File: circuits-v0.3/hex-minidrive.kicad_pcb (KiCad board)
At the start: 4 copper layers, 18 x 48 mm, 81 parts, among them X1 16MHz

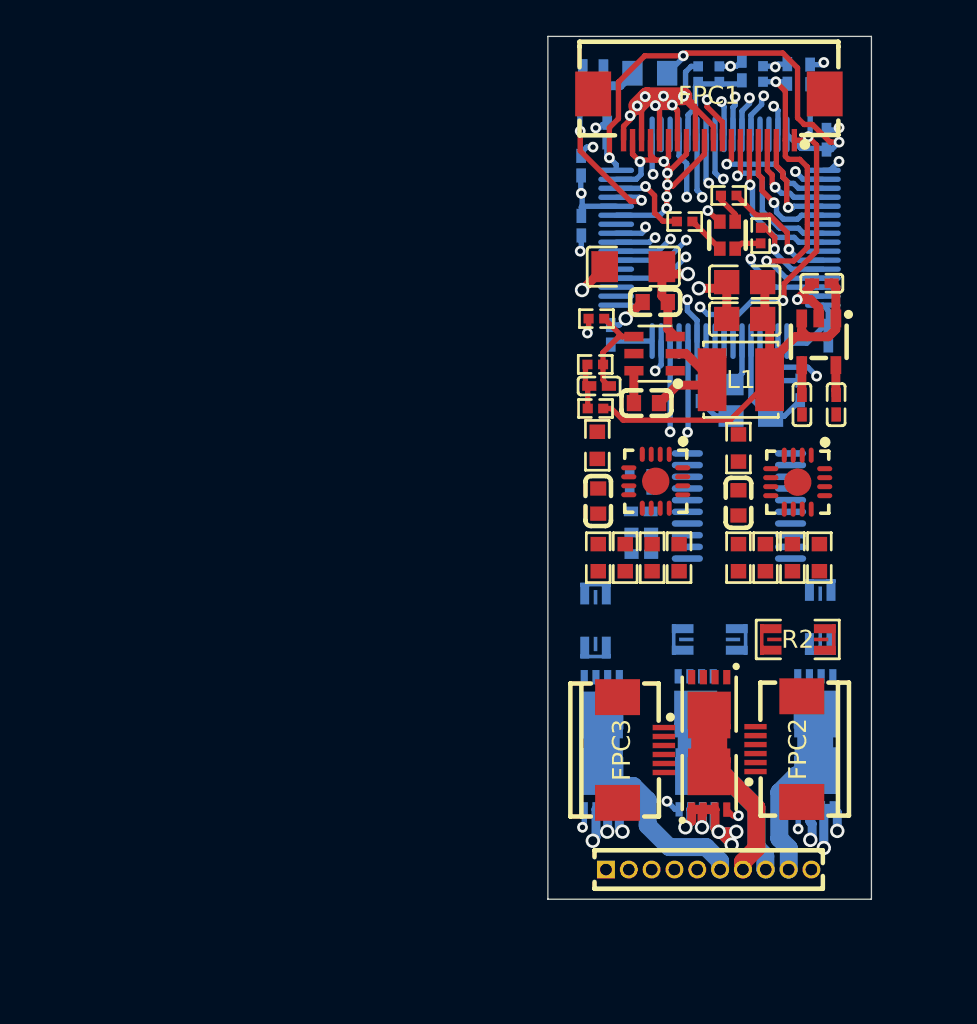
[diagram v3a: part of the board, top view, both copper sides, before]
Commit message: Sketch out route for all crossing wires.
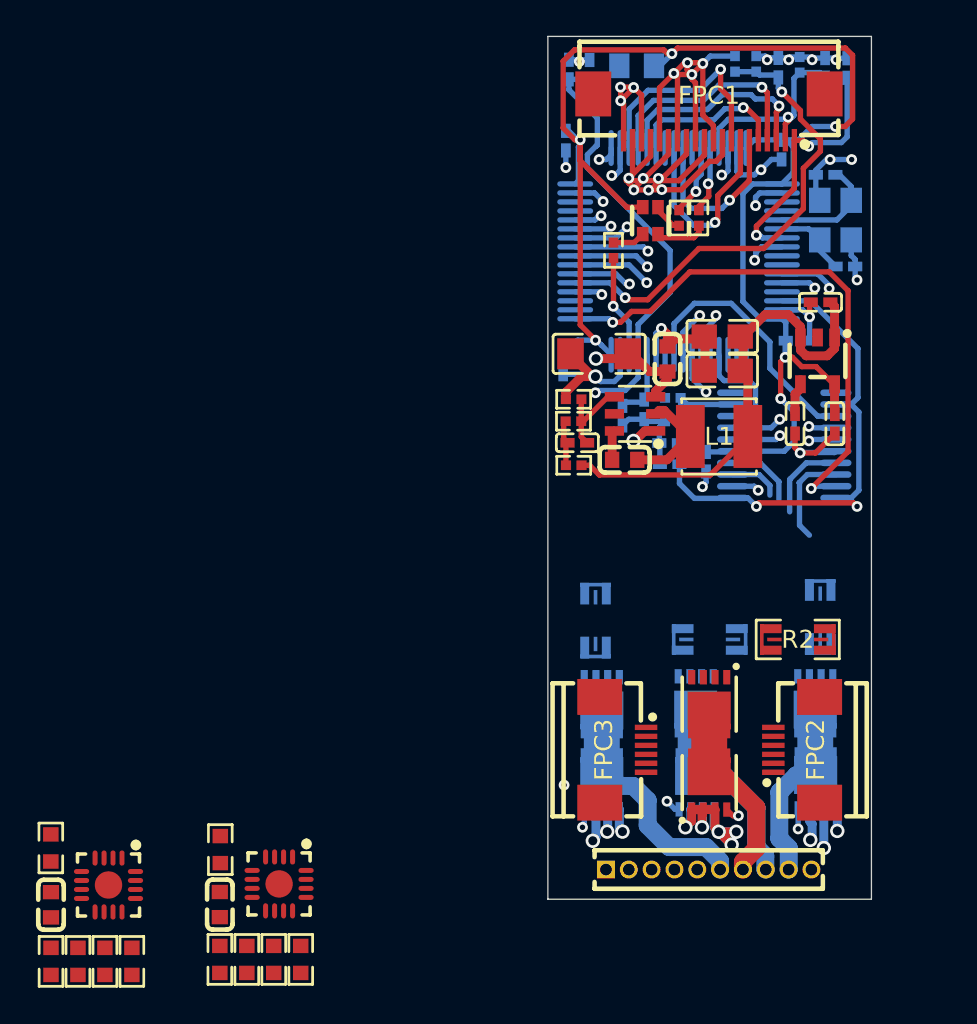
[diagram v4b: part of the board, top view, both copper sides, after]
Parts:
- moved C501 37.8 mm to (-8.64, 68.3)
- moved R101 37.8 mm to (-7.14, 71.5)
- moved R102 37.8 mm to (-8.64, 71.5)
- moved R201 37.8 mm to (-4.14, 71.5)
- moved R202 37.8 mm to (-5.64, 71.5)
- moved U5 37.8 mm to (-5.44, 67.2)
- moved R501 37.8 mm to (-8.65, 65.2)
- moved U6 36.5 mm to (4.05, 67.2)
- moved C601 36.5 mm to (0.75, 68.3)
- moved R301 36.5 mm to (2.25, 71.3)
- moved R302 36.5 mm to (0.75, 71.3)
- moved R401 36.5 mm to (5.25, 71.3)
- moved R402 36.5 mm to (3.75, 71.3)
- moved R601 36.5 mm to (0.78, 65.2)
- moved C109 14.5 mm to (20.0, 25.8), turned to 90 degrees
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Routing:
- net 3V3: track 36.6 -> 88.9 mm, vias 4 -> 6
- net SYS_JTCK-SWCLK: track 1.71 -> 37.5 mm, vias 1 -> 2
- net SYS_JTMS-SVDIO: track 1.10 -> 35.5 mm
- net ADC1_IN3/HALF_VREF: track 5.05 -> 35.7 mm, vias 1 -> 2
- net GND: track 49.4 -> 79.3 mm, vias 21 -> 23
- net ADC2_IN14/M4_CURRENT: track 2.24 -> 30.1 mm, vias 1 -> 2
- net ADC2_IN15/VOLTAGE: track 5.52 -> 26.4 mm, vias 0 -> 2
- net I2C2_SDA: track 2.13 -> 19.5 mm
- net TIM1_CH2: track 2.20 -> 18.5 mm
- net TIM1_CH4: track 2.52 -> 18.8 mm
- net I2C3_SDA: track 1.90 -> 18.1 mm
- net TIM1_CH3: track 2.44 -> 17.9 mm
- net I2C3_SCL: track 2.74 -> 18.1 mm
- net TIM3_CH2/ENCODER_2: track 2.78 -> 17.2 mm
- net TIM1_CH3N: track 4.84 -> 19.3 mm
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
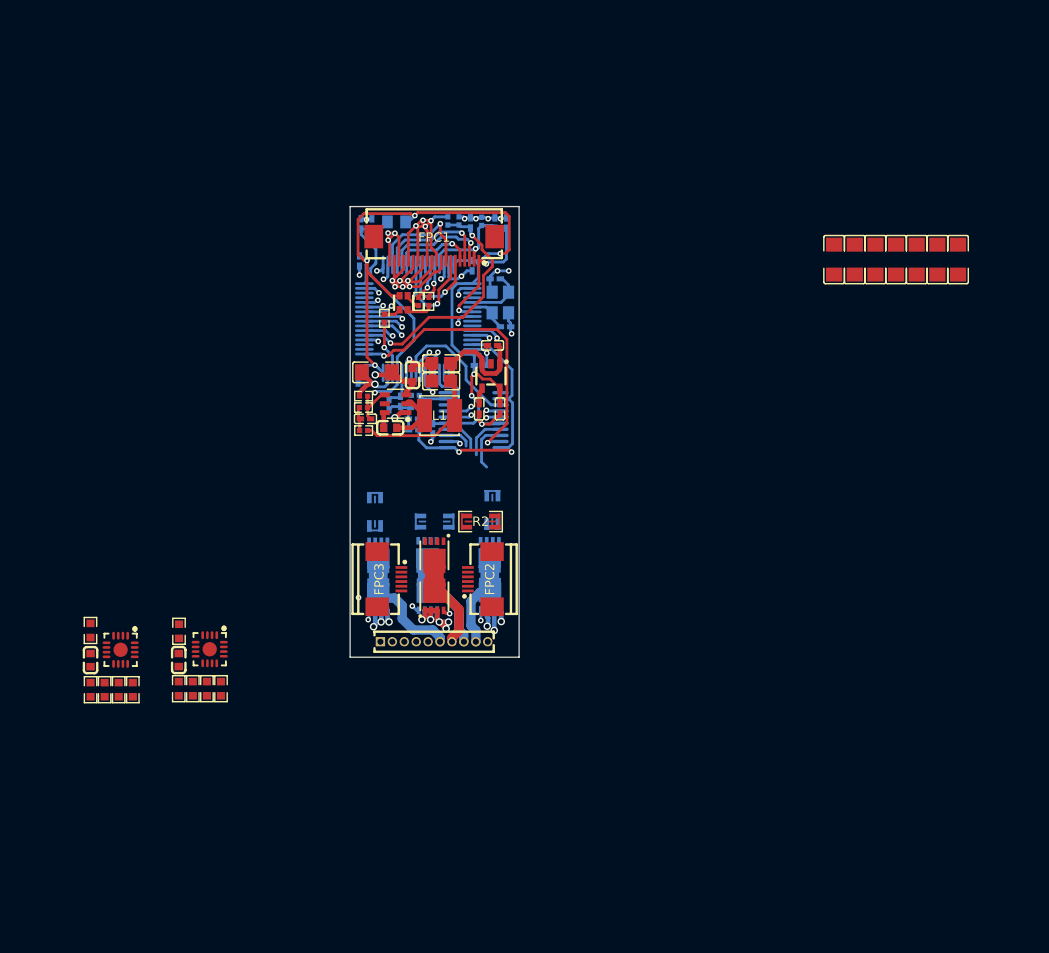
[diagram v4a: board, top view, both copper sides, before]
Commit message: Almost done wiring, but paths need refining.
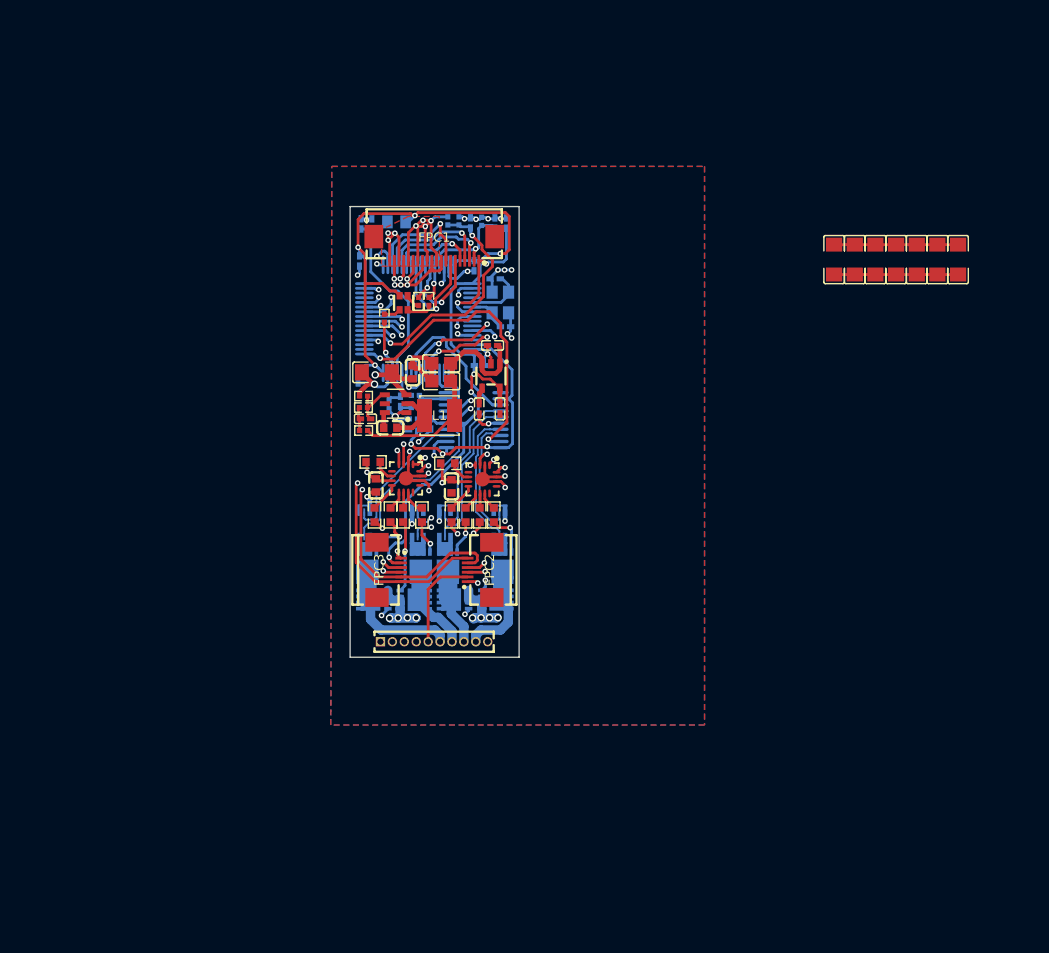
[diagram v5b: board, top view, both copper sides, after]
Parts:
- Q3, Q4, R2: moved to B.Cu
- moved R201 36.0 mm to (26.6, 52.9)
- moved R101 35.7 mm to (23.3, 52.9)
- moved C501 35.6 mm to (21.8, 49.7)
- moved R202 35.6 mm to (24.6, 52.9)
- moved R102 35.5 mm to (21.6, 52.9)
- moved U5 35.5 mm to (24.9, 49.0)
- moved R501 35.0 mm to (21.4, 47.2), turned to 0 degrees
- moved C601 34.4 mm to (29.8, 49.8)
- moved R301 34.4 mm to (31.3, 52.9)
- moved R302 34.4 mm to (29.8, 52.9)
- moved R401 34.4 mm to (34.3, 52.9)
- moved R402 34.4 mm to (32.8, 52.9)
- moved U6 34.2 mm to (33.1, 49.0)
- moved R601 33.8 mm to (29.4, 47.4), turned to 0 degrees
- moved R2 6.71 mm to (26.2, 53.9), turned to 90 degrees
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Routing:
- net 3V3: track 88.9 -> 131.6 mm, vias 6 -> 7
- net GND: track 79.3 -> 113.4 mm, vias 23 -> 36
- net I2C2_SDA: track 19.5 -> 50.7 mm, vias 1 -> 2
- net I2C2_SCL: track 10.5 -> 36.0 mm, vias 1 -> 3
- net TIM3_CH2/ENCODER_2: track 17.2 -> 41.3 mm
- net TIM3_CH1/ENCODER_1: track 16.3 -> 39.5 mm
- net TIM3_CH3/ENCODER_3: track 13.7 -> 34.9 mm
- net TIM1_CH4N: track 7.02 -> 27.7 mm, vias 1 -> 3
- net TIM1_CH3: track 17.9 -> 36.5 mm, vias 1 -> 2
- net I2C3_SCL: track 18.1 -> 35.4 mm, vias 1 -> 2
- net I2C3_SDA: track 18.1 -> 35.4 mm, vias 1 -> 2
- net +Probe-1: track 3.98 -> 19.0 mm
- net SYS_JTMS-SVDIO: track 35.5 -> 49.1 mm, vias 1 -> 2
- net TIM1_CH1N: track 17.5 -> 30.4 mm, vias 1 -> 2
- net SYS_JTCK-SWCLK: track 37.5 -> 50.1 mm
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- added copper zone on B.Cu, net GND
- added copper zone on F.Cu, net GND
- added copper zone on In2.Cu, net GND
- added copper zone on F.Cu, net VCC
- added copper zone on In1.Cu, net VCC
- removed copper zone on In1.Cu, net GND
- removed copper zone on In2.Cu, net VCC

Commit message: More circuit progress, there are ground islands, hmm.
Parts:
- moved C102 23.0 mm to (20.6, 44.9), turned to 180 degrees
- moved C101 21.9 mm to (20.6, 43.7), turned to 180 degrees
- moved L2 19.9 mm to (20.4, 41.2), turned to -90 degrees
- moved R19 10.1 mm to (20.5, 22.2), turned to 0 degrees
- moved C115 9.53 mm to (22.3, 22.1)
- moved R18 9.12 mm to (20.5, 23.7), turned to 0 degrees
- moved C113 0.80 mm to (20.6, 38.2)
- moved C111 0.76 mm to (31.9, 25.6), turned to 180 degrees
- moved C31 0.16 mm to (34.2, 35.0)
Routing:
- net 3V3: track 131.6 -> 108.2 mm, vias 7 -> 5
- net GND: track 113.4 -> 126.4 mm
- net 3V3A: track 21.1 -> 9.34 mm
- net ADC2_IN15/VOLTAGE: track 26.4 -> 17.2 mm
- net TIM1_CH2N: track 24.9 -> 15.8 mm
- net TIM1_CH1N: track 30.4 -> 23.8 mm, vias 2 -> 3
- net VCC: track 75.4 -> 71.6 mm, vias 18 -> 17
- net SPI3_SCK: track 11.8 -> 8.45 mm
- net USART3_TX: track 12.5 -> 15.7 mm
- net I2C2_SCL: track 36.0 -> 38.9 mm
- net SPI3_MOSI: track 8.79 -> 11.5 mm
- net USART3_RX: track 11.7 -> 14.2 mm
- net TIM1_CH3: track 36.5 -> 34.0 mm
- net I2C2_SDA: track 50.7 -> 48.4 mm
- net SPI3_MISO: track 10.5 -> 8.59 mm
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
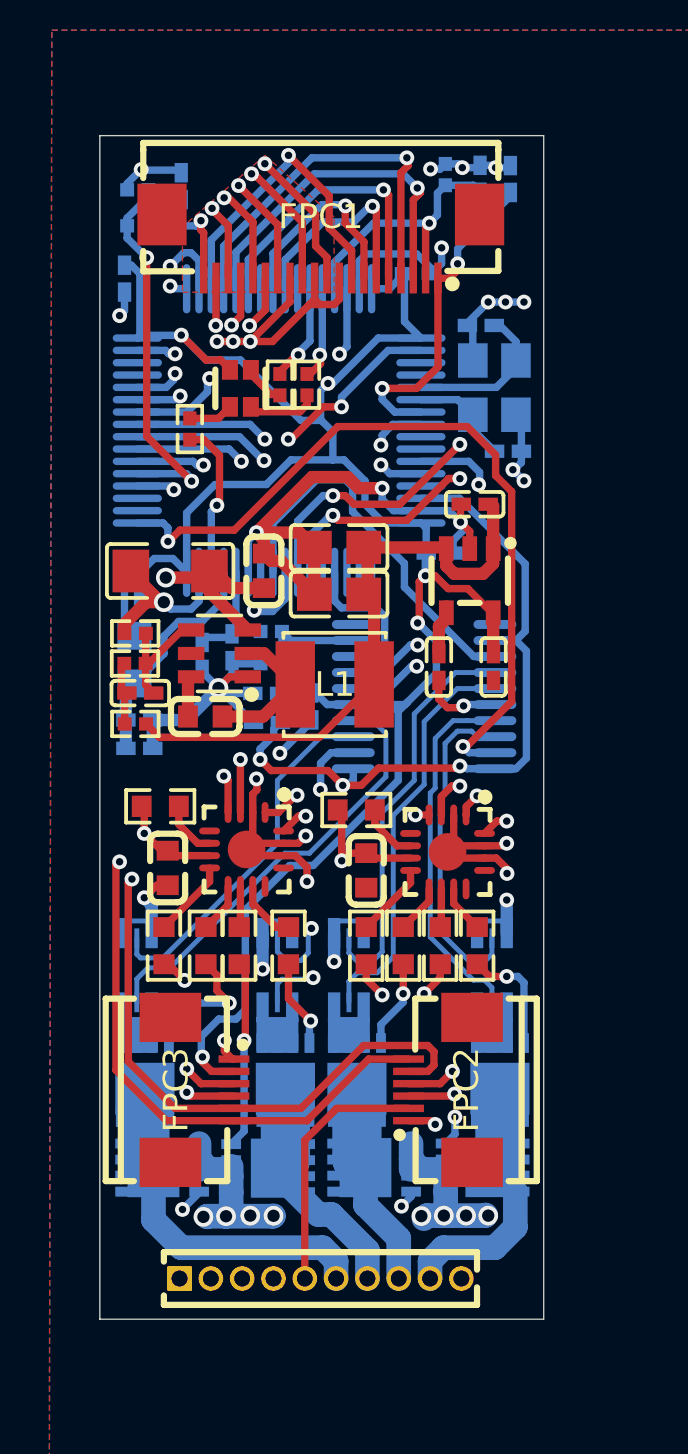
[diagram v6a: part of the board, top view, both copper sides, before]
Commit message: Optimized routing, but we need to go tighter.
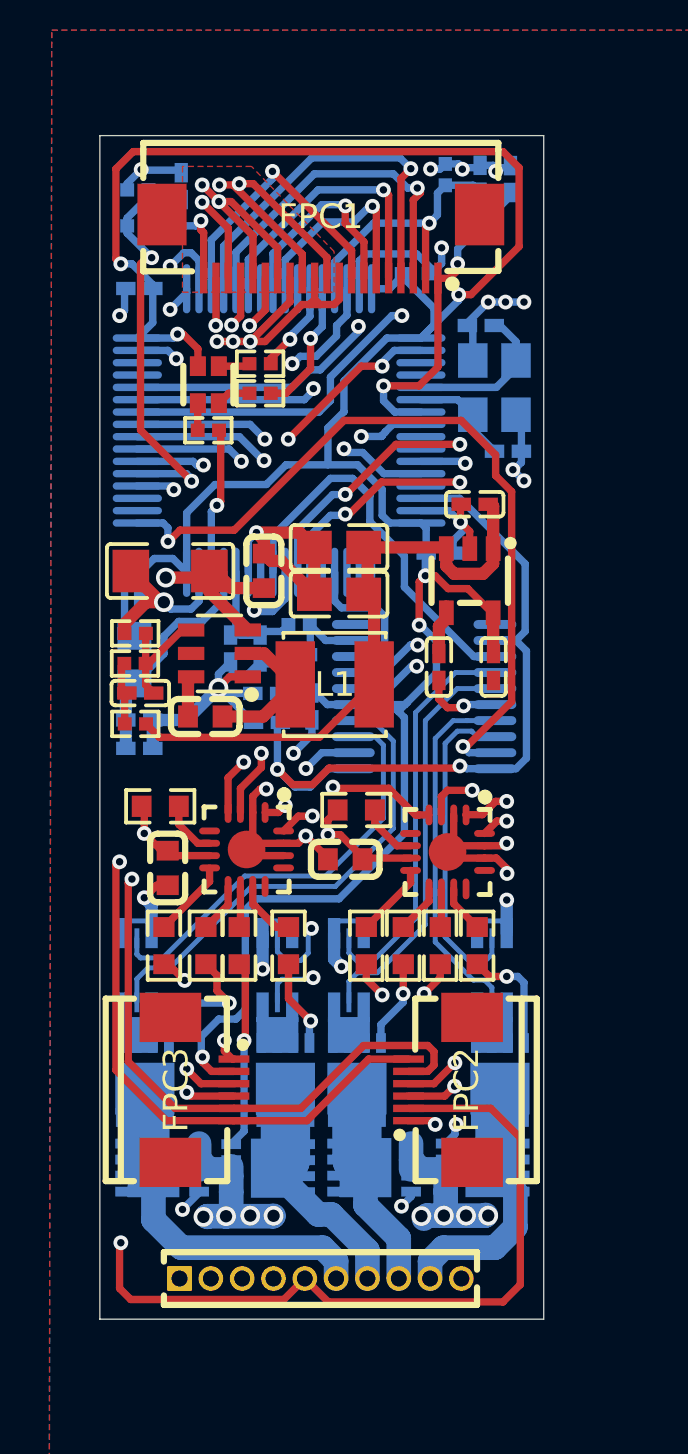
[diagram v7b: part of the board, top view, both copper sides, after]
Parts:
- moved R15 1.93 mm to (25.5, 30.4), turned to 0 degrees
- moved LED1 1.31 mm to (23.4, 30.1)
- moved R12 1.21 mm to (27.1, 41.0)
- moved C105 1.19 mm to (24.3, 40.8)
- moved R17 1.17 mm to (25.5, 29.2), turned to 180 degrees
- moved R13 1.16 mm to (27.1, 39.8)
- moved C106 1.14 mm to (25.5, 40.8)
- moved C601 0.96 mm to (28.9, 49.4), turned to 0 degrees
- moved R16 0.75 mm to (23.4, 31.9), turned to 0 degrees
- moved C109 0.72 mm to (20.6, 26.2), turned to 0 degrees
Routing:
- net 3V3: track 108.2 -> 152.0 mm, vias 5 -> 7
- net GND: track 126.4 -> 119.4 mm, vias 36 -> 34
- net TIM1_CH2: track 25.7 -> 30.3 mm
- net TIM1_CH3N: track 25.1 -> 29.6 mm
- net I2C2_SCL: track 38.9 -> 35.3 mm
- net -Probe-1: track 14.7 -> 17.4 mm
- net ADC1_IN3/HALF_VREF: track 35.8 -> 37.5 mm, vias 3 -> 2
- net +Probe-1: track 17.7 -> 19.4 mm
- net TIM4_CH2/GREEN_LED: track 3.82 -> 5.47 mm
- net /Green-LED: track 2.86 -> 1.41 mm
- net VCC: track 71.6 -> 72.9 mm
- net SPI3_NSS: track 12.7 -> 11.4 mm
- net I2C2_SDA: track 48.4 -> 49.6 mm
- net TIM1_CH2N: track 15.8 -> 16.9 mm
- net VREF: track 5.11 -> 5.92 mm
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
